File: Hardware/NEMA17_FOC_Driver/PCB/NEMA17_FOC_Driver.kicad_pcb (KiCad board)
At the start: 2 copper layers, 42 x 42 mm, 37 parts, among them J1 Conn_01x02_Pin, J2 Conn_01x02_Pin, U1 DRV8844PWPR, U2 AP63203WU-7, U3 MT6701CT, U4 STM32G431KBTx, U5 TCAN332

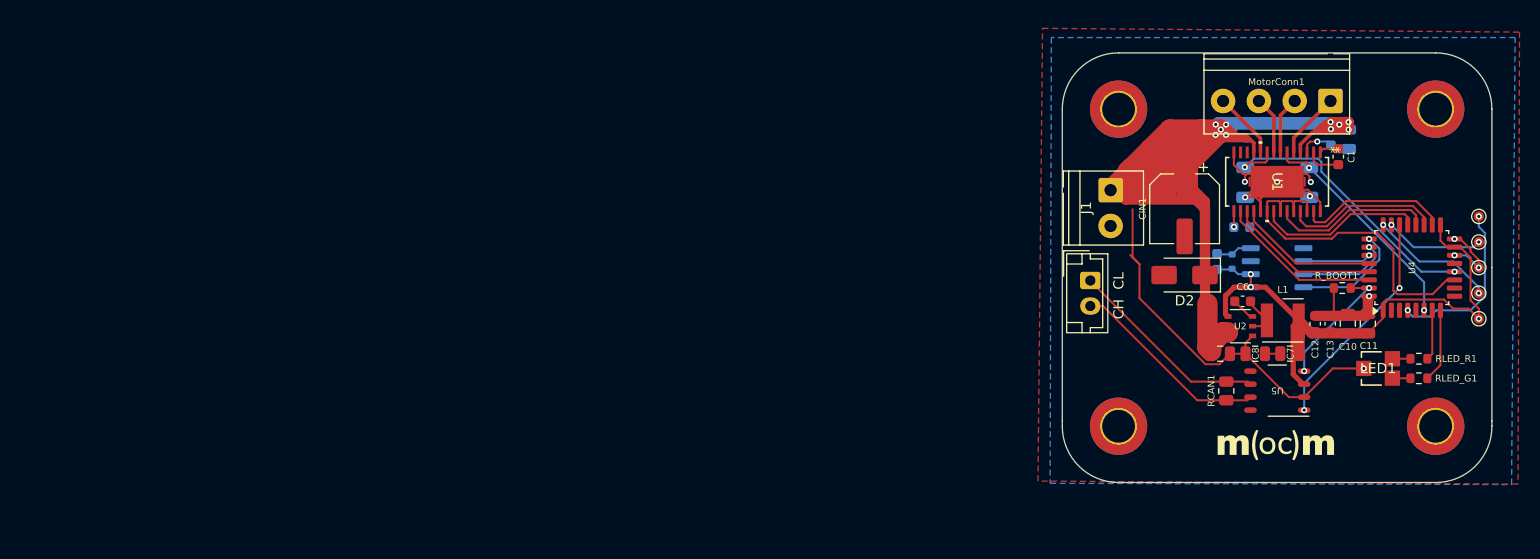
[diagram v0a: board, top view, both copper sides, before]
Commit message: Firmware structure, schematic for PCB V2.0, layout still pending.
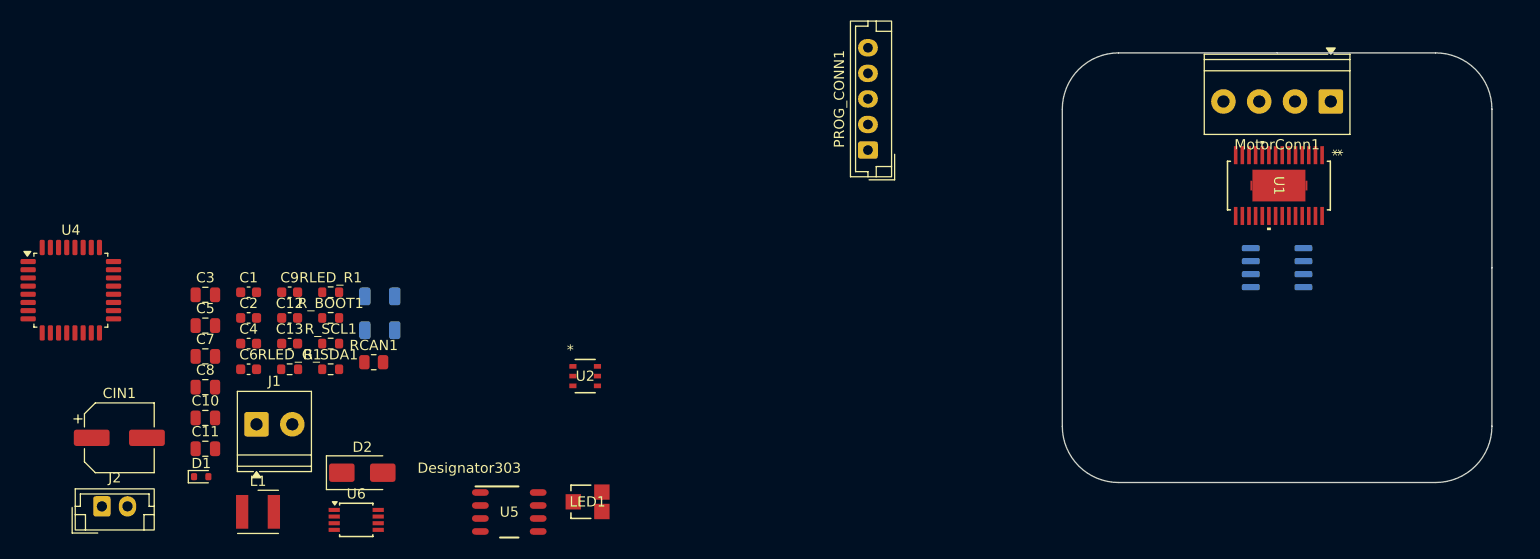
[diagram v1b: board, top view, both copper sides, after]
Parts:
- removed REF** (x4): MountingHole_3.2mm_M3_DIN965_Pad_TopBottom, MountingHole:MountingHole_3.2mm_M3_DIN965_Pad_TopBottom
- removed REF**: TestPoint_Pad_D1.0mm, TestPoint:TestPoint_Pad_D1.0mm
- added PROG_CONN1: Conn_01x05_Pin, Connector_JST:JST_EH_B5B-EH-A_1x05_P2.50mm_Vertical, F.Cu at (125.5, 63.0)
- added R_SCL1: 10k, Resistor_SMD:R_0603_1608Metric, F.Cu at (73.0, 81.9)
- added R_SDA1: 10k, Resistor_SMD:R_0603_1608Metric, F.Cu at (73.0, 84.4)
- added U6: 24LC64, Package_SO:TSSOP-8_3x3mm_P0.65mm, F.Cu at (75.5, 99.2)
- C2, C3, C4, C9, D1, MotorConn1: moved to F.Cu
- LED1: footprint SML:SML-LX15_LUM -> SML-LX15:SML-LX15_LUM
- U1: footprint DRV8844:PWP28_5P18X3P1-L -> DRV8844:PWP28_5P18X3P1-M
- U2: footprint AP63203:AP63203WU-7_DIO-L -> AP63203WU:AP63203WU-7_DIO-L
- U5: footprint TCAN332:D0008A_L -> TCAN332:D0008A_M
- moved U4 131.1 mm to (47.6, 76.7), turned to 0 degrees
- moved C11 114.3 mm to (60.7, 92.2), turned to 0 degrees
- moved C3 112.8 mm to (60.7, 77.2), turned to 0 degrees
- moved C10 112.1 mm to (60.7, 89.2), turned to 0 degrees
- moved RLED_G1 110.4 mm to (69.0, 84.4)
- moved C1 107.3 mm to (65.0, 76.9), turned to 0 degrees
- moved C2 107.3 mm to (65.0, 79.4), turned to 0 degrees
- moved RLED_R1 106.6 mm to (73.0, 76.9), turned to 0 degrees
- moved CIN1 106.5 mm to (52.3, 91.1), turned to 0 degrees
- moved C7 106.0 mm to (60.7, 83.2), turned to 0 degrees
- moved D1 103.0 mm to (60.3, 94.9), turned to 0 degrees
- moved C8 102.7 mm to (60.7, 86.2), turned to 0 degrees
- moved L1 101.9 mm to (65.9, 98.4)
- moved C13 101.7 mm to (69.0, 81.9), turned to 0 degrees
- moved C12 100.3 mm to (69.0, 79.4), turned to 0 degrees
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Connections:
- C7 pad 2: Net-(C7-Pad2) -> GND
- C8 pad 1: Net-(C7-Pad2) -> +3.3V
- U1 pad 17: nSLEEP -> nRESET
- U4 pad 11: EN -> unconnected-(U4-PA6-Pad11)
- U4 pad 2: unconnected-(U4-PF0-Pad2) -> EN
- U4 pad 25: ChipSelect -> SCL
- U4 pad 28: nFAULT -> ChipSelect
- U4 pad 29: nSLEEP -> unconnected-(U4-PB6-Pad29)
- U4 pad 3: unconnected-(U4-PF1-Pad3) -> nRESET
- U4 pad 30: nRESET -> SDA
- U4 pad 5: unconnected-(U4-PA0-Pad5) -> nFAULT
- U4 pad 7: LEDPIN_R -> LEDPIN_G
- U4 pad 8: LEDPIN_G -> LEDPIN_R
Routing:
- net +12V: track 171.4 -> 0.00 mm, vias 10 -> 0
- net GND: track 100.2 -> 0.00 mm, vias 10 -> 0
- net +3.3V: track 73.6 -> 0.00 mm, vias 3 -> 0
- net EN: track 35.2 -> 0.00 mm
- net SRC34: track 29.3 -> 0.00 mm, vias 2 -> 0
- net SRC12: track 22.1 -> 0.00 mm, vias 2 -> 0
- net TXD: track 22.0 -> 0.00 mm, vias 2 -> 0
- net CAN Low: track 19.9 -> 0.00 mm
- net CAN High: track 19.6 -> 0.00 mm
- net NRST: track 16.7 -> 0.00 mm, vias 2 -> 0
- net IN4: track 16.3 -> 0.00 mm
- net nRESET: track 15.9 -> 0.00 mm
- net IN3: track 15.7 -> 0.00 mm
- net IN2: track 15.2 -> 0.00 mm
- net nSLEEP: track 14.9 -> 0.00 mm
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- removed copper zone on B.Cu, net GND
- removed copper zone on F.Cu, net GND
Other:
- outline, holes or cut-outs redrawn
- board text removed: "12V"
- board text removed: "3.3V"
- board text removed: "CH"
- board text removed: "CL"
- board text removed: "GND"
- board text removed: "NRST"
- board text removed: "SWCLK"
- board text removed: "SWDIO"
